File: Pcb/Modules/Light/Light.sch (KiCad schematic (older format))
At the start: 20 parts, among them J1 JACK_RJ45, J2 JACK_STEREO, Q1 TEPT4400, Q2 Q_NMOS_GSD, U1 74LVC1G07, U2 74LVC1G07

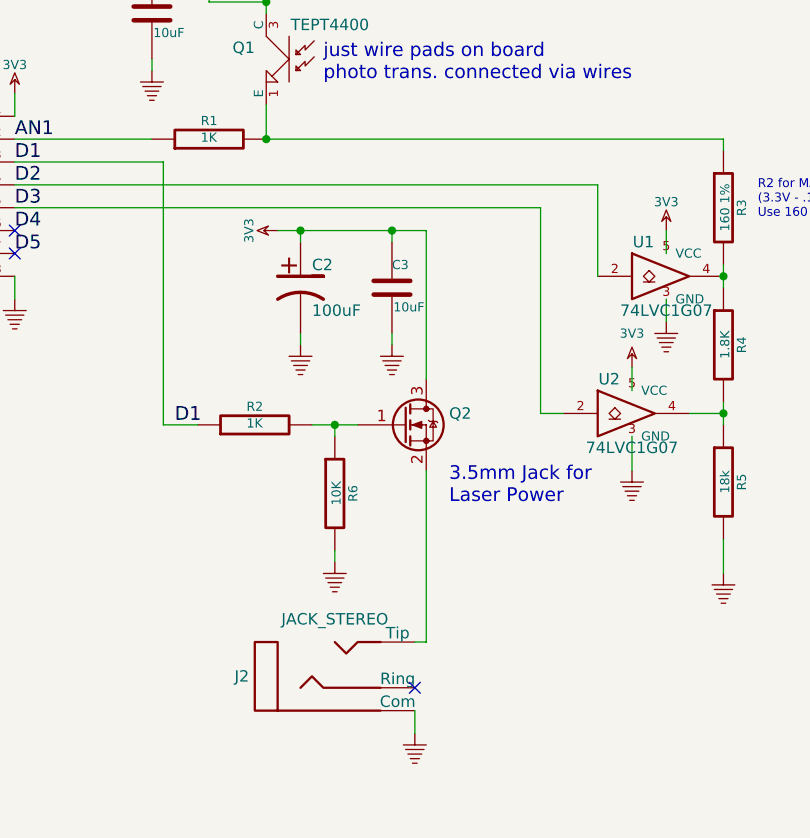
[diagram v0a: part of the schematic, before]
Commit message: Update PCBs to use n channel mosfet on low side
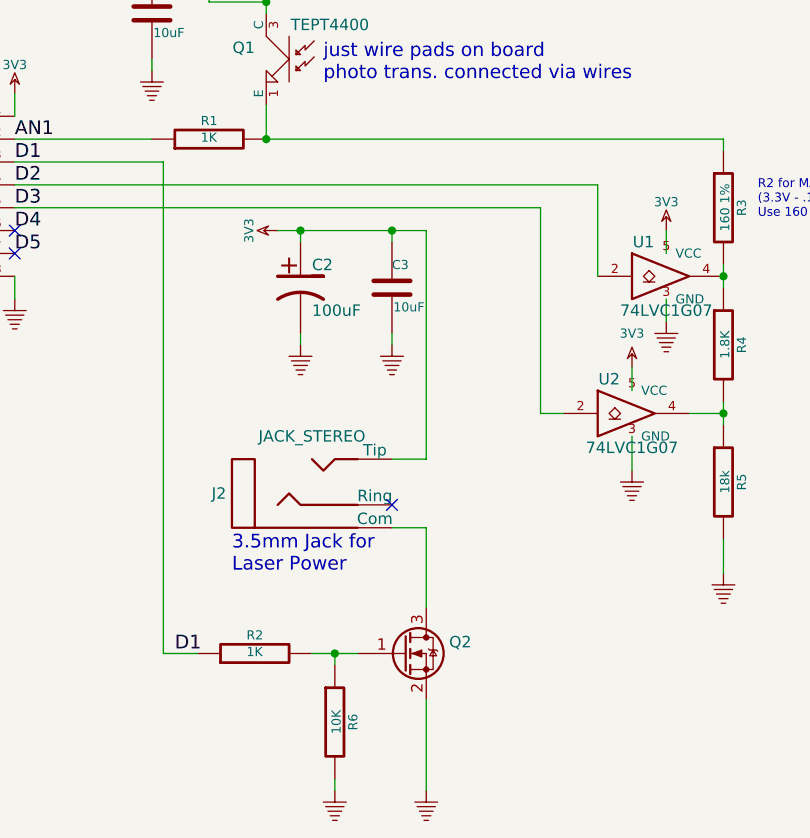
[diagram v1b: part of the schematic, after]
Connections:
- net 3V3: now also J2.2 (Tip); no longer Q2.3 (D)
- net GND: now also Q2.2 (S); no longer J2.3 (Com)
- new net: J2.3 (Com), Q2.3 (D)
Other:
- moved on the sheet: J2, Q2, R2, R6
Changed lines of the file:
@@
 L JACK_STEREO J2
 U 1 1 54012E4D
-P 6050 5750
-F 0 "J2" H 5675 5750 50  0000 R CNN
-F 1 "JACK_STEREO" H 6050 6000 50  0000 C CNN
-F 2 "CA6:161-3334-E_Big_Pad" H 6050 5750 60  0001 C CNN
-F 3 "~" H 6050 5750 60  0000 C CNN
-	1    6050 5750
+P 5950 4950
+F 0 "J2" H 5575 4950 50  0000 R CNN
+F 1 "JACK_STEREO" H 5950 5200 50  0000 C CNN
+F 2 "CA6:161-3334-E_Big_Pad" H 5950 4950 60  0001 C CNN
+F 3 "~" H 5950 4950 60  0000 C CNN
+	1    5950 4950
 	1    0    0    -1
 $EndComp
@@
 $EndComp
 $Comp
-L 3V3 #PWR3
+L 3V3 #PWR01
 U 1 1 540144B1
 P 4650 3200
-F 0 "#PWR3" H 4650 3300 40  0001 C CNN
+F 0 "#PWR01" H 4650 3300 40  0001 C CNN
 F 1 "3V3" H 4650 3325 40  0000 C CNN
 F 2 "" H 4650 3200 60  0000 C CNN
@@
 D5
 $Comp
-L GND #PWR4
+L GND #PWR02
 U 1 1 540144C2
 P 4650 4100
-F 0 "#PWR4" H 4650 4100 30  0001 C CNN
+F 0 "#PWR02" H 4650 4100 30  0001 C CNN
 F 1 "GND" H 4650 4030 30  0001 C CNN
 F 2 "" H 4650 4100 60  0000 C CNN
@@
 	4650 3200 4650 3300
 $Comp
-L 3V3 #PWR7
+L 3V3 #PWR03
 U 1 1 5401450D
 P 5800 3800
-F 0 "#PWR7" H 5800 3900 40  0001 C CNN
+F 0 "#PWR03" H 5800 3900 40  0001 C CNN
 F 1 "3V3" H 5800 3925 40  0000 C CNN
 F 2 "" H 5800 3800 60  0000 C CNN
@@
 Wire Wire Line
 	4650 4000 4650 4100
-Text Label 5350 4650 0    60   ~ 0
+Text Label 5350 5650 0    60   ~ 0
 D1
 $Comp
 L R R2
 U 1 1 54AA118B
-P 5700 4650
-F 0 "R2" V 5780 4650 40  0000 C CNN
-F 1 "1K" V 5707 4651 40  0000 C CNN
-F 2 "CA6:SM0603_Resistor" V 5630 4650 30  0001 C CNN
-F 3 "~" H 5700 4650 30  0000 C CNN
-	1    5700 4650
+P 5700 5650
+F 0 "R2" V 5780 5650 40  0000 C CNN
+F 1 "1K" V 5707 5651 40  0000 C CNN
+F 2 "CA6:SM0603_Resistor" V 5630 5650 30  0001 C CNN
+F 3 "~" H 5700 5650 30  0000 C CNN
+	1    5700 5650
 	0    -1   -1   0
 $EndComp
@@
 $EndComp
 $Comp
-L 3V3 #PWR6
+L 3V3 #PWR04
 U 1 1 54AA199D
 P 5750 2750
-F 0 "#PWR6" H 5750 2850 40  0001 C CNN
+F 0 "#PWR04" H 5750 2850 40  0001 C CNN
 F 1 "3V3" H 5750 2875 40  0000 C CNN
 F 2 "" H 5750 2750 60  0000 C CNN
@@
 $EndComp
 $Comp
-L GND #PWR16
+L GND #PWR05
 U 1 1 54AA1A1B
 P 7750 5300
-F 0 "#PWR16" H 7750 5300 30  0001 C CNN
+F 0 "#PWR05" H 7750 5300 30  0001 C CNN
 F 1 "GND" H 7750 5230 30  0001 C CNN
 F 2 "" H 7750 5300 60  0000 C CNN
@@
 	1    0    0    -1
 $EndComp
-Text Notes 6550 5000 0    60   ~ 0
+Text Notes 5600 5300 0    60   ~ 0
 3.5mm Jack for\nLaser Power
 Text Notes 3900 2450 0    60   ~ 0
@@
 $EndComp
 $Comp
-L GND #PWR5
+L GND #PWR06
 U 1 1 54AABCE0
 P 5250 3100
-F 0 "#PWR5" H 5250 3100 30  0001 C CNN
+F 0 "#PWR06" H 5250 3100 30  0001 C CNN
 F 1 "GND" H 5250 3030 30  0001 C CNN
 F 2 "" H 5250 3100 60  0000 C CNN
@@
 	4650 3400 5250 3400
 Wire Wire Line
-	5300 3500 5300 4650
+	5300 3500 5300 5650
 Wire Wire Line
 	5300 3500 4650 3500
 NoConn ~ 4650 3800
 NoConn ~ 4650 3900
-NoConn ~ 6400 5800
-$Comp
-L PWR_FLAG #FLG2
+$Comp
+L PWR_FLAG #FLG07
 U 1 1 58FEFDE5
 P 4300 2950
-F 0 "#FLG2" H 4300 3025 50  0001 C CNN
+F 0 "#FLG07" H 4300 3025 50  0001 C CNN
 F 1 "PWR_FLAG" H 4300 3100 50  0000 C CNN
 F 2 "" H 4300 2950 50  0001 C CNN
@@
 $EndComp
 $Comp
-L 3V3 #PWR2
+L 3V3 #PWR08
 U 1 1 58FEFE63
 P 4300 2850
-F 0 "#PWR2" H 4300 2950 40  0001 C CNN
+F 0 "#PWR08" H 4300 2950 40  0001 C CNN
 F 1 "3V3" H 4300 2975 40  0000 C CNN
 F 2 "" H 4300 2850 60  0000 C CNN
@@
 just wire pads on board\nphoto trans. connected via wires
 Wire Wire Line
-	6150 4650 5950 4650
-Wire Wire Line
-	6450 4850 6450 5600
-Wire Wire Line
-	5300 4650 5450 4650
+	5950 5650 6150 5650
+Wire Wire Line
+	5300 5650 5450 5650
 Text Notes 7900 3750 0    39   ~ 0
 R2 for MAX current of 20mA\n(3.3V - .17 drop across Buffer)/20mA=156.5 ohms\nUse 160 ohms for max current = 19.5 mA
 $Comp
-L PWR_FLAG #FLG1
+L PWR_FLAG #FLG09
 U 1 1 59E23186
 P 4200 4350
-F 0 "#FLG1" H 4200 4425 50  0001 C CNN
+F 0 "#FLG09" H 4200 4425 50  0001 C CNN
 F 1 "PWR_FLAG" H 4200 4500 50  0000 C CNN
 F 2 "" H 4200 4350 50  0001 C CNN
@@
 $EndComp
 $Comp
-L GND #PWR1
+L GND #PWR010
 U 1 1 59E231B3
 P 4200 4450
-F 0 "#PWR1" H 4200 4450 30  0001 C CNN
+F 0 "#PWR010" H 4200 4450 30  0001 C CNN
 F 1 "GND" H 4200 4380 30  0001 C CNN
 F 2 "" H 4200 4450 60  0000 C CNN
@@
 L Q_NMOS_GSD Q2
 U 1 1 59E3F4ED
-P 6350 4650
-F 0 "Q2" H 6550 4700 50  0000 L CNN
-F 1 "Q_NMOS_GSD" H 6550 4600 50  0001 L CNN
-F 2 "TO_SOT_Packages_SMD:SOT-23" H 6550 4750 50  0001 C CNN
-F 3 "" H 6350 4650 50  0000 C CNN
-	1    6350 4650
+P 6350 5650
+F 0 "Q2" H 6550 5700 50  0000 L CNN
+F 1 "Q_NMOS_GSD" H 6550 5600 50  0001 L CNN
+F 2 "TO_SOT_Packages_SMD:SOT-23" H 6550 5750 50  0001 C CNN
+F 3 "" H 6350 5650 50  0000 C CNN
+	1    6350 5650
 	1    0    0    -1
 $EndComp
@@
 	6950 3700 4650 3700
 $Comp
-L GND #PWR13
+L GND #PWR011
 U 1 1 5A247E92
 P 7350 4850
-F 0 "#PWR13" H 7350 4850 30  0001 C CNN
+F 0 "#PWR011" H 7350 4850 30  0001 C CNN
 F 1 "GND" H 7350 4780 30  0001 C CNN
 F 2 "" H 7350 4850 60  0000 C CNN
@@
 $EndComp
 $Comp
-L GND #PWR15
+L GND #PWR012
 U 1 1 5A247ECA
 P 7500 4200
-F 0 "#PWR15" H 7500 4200 30  0001 C CNN
+F 0 "#PWR012" H 7500 4200 30  0001 C CNN
 F 1 "GND" H 7500 4130 30  0001 C CNN
 F 2 "" H 7500 4200 60  0000 C CNN
@@
 $EndComp
 $Comp
-L 3V3 #PWR14
+L 3V3 #PWR013
 U 1 1 5A248403
 P 7500 3800
-F 0 "#PWR14" H 7500 3900 40  0001 C CNN
+F 0 "#PWR013" H 7500 3900 40  0001 C CNN
 F 1 "3V3" H 7500 3925 40  0000 C CNN
 F 2 "" H 7500 3800 60  0000 C CNN
@@
 $EndComp
 $Comp
-L 3V3 #PWR12
+L 3V3 #PWR014
 U 1 1 5A2484A4
 P 7350 4400
-F 0 "#PWR12" H 7350 4500 40  0001 C CNN
+F 0 "#PWR014" H 7350 4500 40  0001 C CNN
 F 1 "3V3" H 7350 4550 40  0000 C CNN
 F 2 "" H 7350 4400 60  0000 C CNN
@@
 	5800 3800 6450 3800
 Wire Wire Line
-	6450 3800 6450 4450
+	6450 3800 6450 4800
 Wire Wire Line
 	6300 3850 6300 3800
@@
 Connection ~ 5900 3800
 $Comp
-L GND #PWR8
+L GND #PWR015
 U 1 1 5A2880E8
 P 5900 4300
-F 0 "#PWR8" H 5900 4300 30  0001 C CNN
+F 0 "#PWR015" H 5900 4300 30  0001 C CNN
 F 1 "GND" H 5900 4230 30  0001 C CNN
 F 2 "" H 5900 4300 60  0000 C CNN
@@
 $EndComp
 $Comp
-L GND #PWR10
+L GND #PWR016
 U 1 1 5A288126
 P 6300 4300
-F 0 "#PWR10" H 6300 4300 30  0001 C CNN
+F 0 "#PWR016" H 6300 4300 30  0001 C CNN
 F 1 "GND" H 6300 4230 30  0001 C CNN
 F 2 "" H 6300 4300 60  0000 C CNN
@@
 $EndComp
 $Comp
-L GND #PWR11
-U 1 1 5401451B
-P 6400 6000
-F 0 "#PWR11" H 6400 6000 30  0001 C CNN
-F 1 "GND" H 6400 5930 30  0001 C CNN
-F 2 "" H 6400 6000 60  0000 C CNN
-F 3 "" H 6400 6000 60  0000 C CNN
-	1    6400 6000
-	1    0    0    -1
-$EndComp
-Wire Wire Line
-	6400 5900 6400 6000
-Wire Wire Line
-	6450 5600 6400 5600
-$Comp
 L R R6
 U 1 1 5A32AF14
-P 6050 4950
-F 0 "R6" V 6130 4950 40  0000 C CNN
-F 1 "10K" V 6057 4951 40  0000 C CNN
-F 2 "CA6:SM0603_Resistor" V 5980 4950 30  0001 C CNN
-F 3 "~" H 6050 4950 30  0000 C CNN
-	1    6050 4950
-	1    0    0    -1
-$EndComp
-Wire Wire Line
-	6050 4700 6050 4650
-Connection ~ 6050 4650
-$Comp
-L GND #PWR9
+P 6050 5950
+F 0 "R6" V 6130 5950 40  0000 C CNN
+F 1 "10K" V 6057 5951 40  0000 C CNN
+F 2 "CA6:SM0603_Resistor" V 5980 5950 30  0001 C CNN
+F 3 "~" H 6050 5950 30  0000 C CNN
+	1    6050 5950
+	1    0    0    -1
+$EndComp
+Wire Wire Line
+	6050 5700 6050 5650
+Connection ~ 6050 5650
+$Comp
+L GND #PWR017
 U 1 1 5A32B0B2
-P 6050 5250
-F 0 "#PWR9" H 6050 5250 30  0001 C CNN
-F 1 "GND" H 6050 5180 30  0001 C CNN
-F 2 "" H 6050 5250 60  0000 C CNN
-F 3 "" H 6050 5250 60  0000 C CNN
-	1    6050 5250
-	1    0    0    -1
-$EndComp
-Wire Wire Line
-	6050 5250 6050 5200
+P 6050 6250
+F 0 "#PWR017" H 6050 6250 30  0001 C CNN
+F 1 "GND" H 6050 6180 30  0001 C CNN
+F 2 "" H 6050 6250 60  0000 C CNN
+F 3 "" H 6050 6250 60  0000 C CNN
+	1    6050 6250
+	1    0    0    -1
+$EndComp
+Wire Wire Line
+	6050 6250 6050 6200
+Wire Wire Line
+	6450 4800 6300 4800
+NoConn ~ 6300 5000
+Wire Wire Line
+	6300 5100 6450 5100
+Wire Wire Line
+	6450 5100 6450 5450
+Wire Wire Line
+	6450 5850 6450 6250
+$Comp
+L GND #PWR018
+U 1 1 5A36EE99
+P 6450 6250
+F 0 "#PWR018" H 6450 6250 30  0001 C CNN
+F 1 "GND" H 6450 6180 30  0001 C CNN
+F 2 "" H 6450 6250 60  0000 C CNN
+F 3 "" H 6450 6250 60  0000 C CNN
+	1    6450 6250
+	1    0    0    -1
+$EndComp
 $EndSCHEMATC
